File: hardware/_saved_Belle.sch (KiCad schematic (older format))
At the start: 23 parts, among them P1 Bell CONN, P2 Battery CONN, P3 FTDI Flashing CONN, P4 Boot JUMPER, U1 74AHC1G14, U2 ESP-12, U3 AP2112

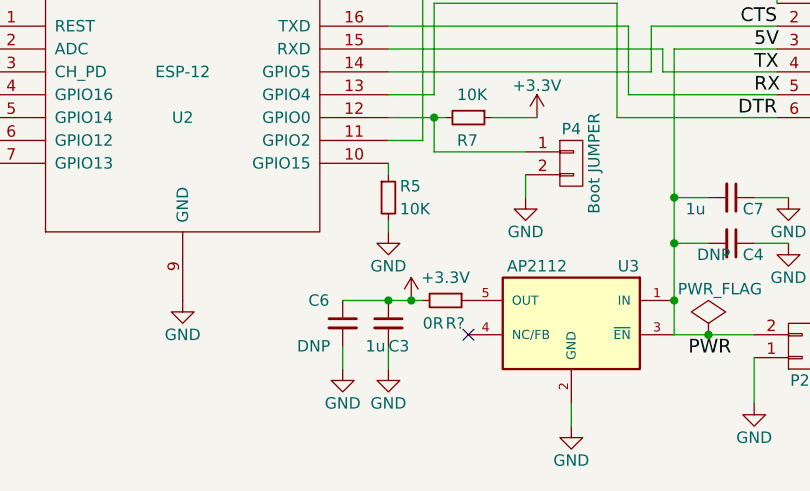
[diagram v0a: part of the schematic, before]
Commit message: add dfm tweaks. #18
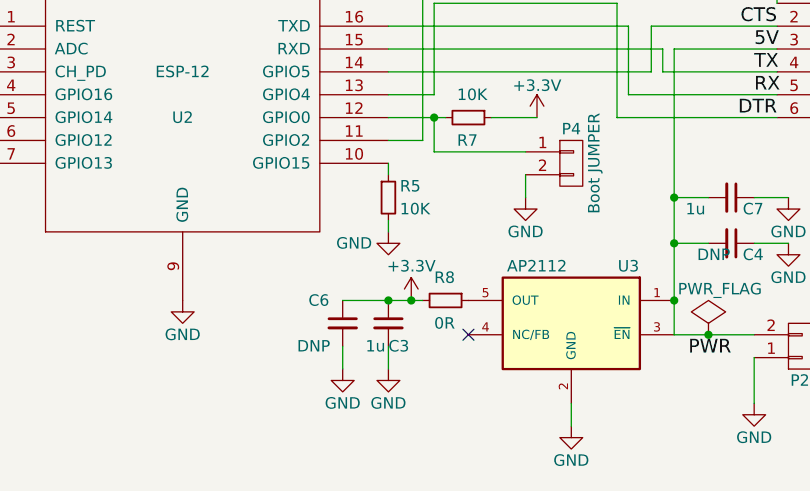
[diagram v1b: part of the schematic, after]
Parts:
- R8: renamed from R?; footprint (none) -> Resistors_SMD:R_1206_HandSoldering
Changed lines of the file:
@@
 P 6800 4400
 F 0 "#PWR011" H 6800 4150 50  0001 C CNN
-F 1 "GND" H 6800 4250 50  0000 C CNN
+F 1 "GND" H 6650 4350 50  0000 C CNN
 F 2 "" H 6800 4400 50  0000 C CNN
 F 3 "" H 6800 4400 50  0000 C CNN
@@
 P 6900 4700
 F 0 "#PWR012" H 6900 4550 50  0001 C CNN
-F 1 "+3.3V" H 6750 4800 50  0000 C CNN
+F 1 "+3.3V" H 6900 4850 50  0000 C CNN
 F 2 "" H 6900 4700 50  0000 C CNN
 F 3 "" H 6900 4700 50  0000 C CNN
@@
 	7800 3900 8500 3900
 $Comp
-L R_Small R?
+L R_Small R8
 U 1 1 5912943F
 P 7050 4700
-F 0 "R?" V 7150 4700 50  0000 L CNN
-F 1 "0R" V 7150 4600 50  0000 L CNN
-F 2 "" H 7050 4700 50  0000 C CNN
+F 0 "R8" V 6950 4650 50  0000 L CNN
+F 1 "0R" V 7150 4650 50  0000 L CNN
+F 2 "Resistors_SMD:R_1206_HandSoldering" H 7050 4700 50  0001 C CNN
 F 3 "" H 7050 4700 50  0000 C CNN
 	1    7050 4700
